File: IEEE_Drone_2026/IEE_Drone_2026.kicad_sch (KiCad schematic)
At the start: 40 parts, among them IC1 TPSM84209RKHT, J1 ESC, J10 M2, J11 Conn_01x02_Socket, J12 RF, J13 USB_C_Receptacle_USB2.0_16P, J2 M4 Mounting, J3 M4 Mounting, J4 M4 Mounting, J5 M4 Mounting, J6 Pixy2, J7 M2, J8 M2, J9 M2, Q1 2N2222, U2 STM32F405RGTx, U3 BMP390, U4 SAM-M10Q-00B, U5 LIS2MDL, Y1 LFXTAL020423, Y2 ABMM2-32.768MHZ-E2F-T

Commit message: wired the imu
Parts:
- added C1: 0.1uF, Capacitor_SMD:C_0603_1608Metric_Pad1.08x0.95mm_HandSolder, symbol Device:C
- added C13: 2.2uF, Capacitor_SMD:C_0603_1608Metric_Pad1.08x0.95mm_HandSolder, symbol Device:C
- added C14: 10nF, Capacitor_SMD:C_0603_1608Metric_Pad1.08x0.95mm_HandSolder, symbol Device:C
- added R6, R8: 5.1k, Resistor_SMD:R_0603_1608Metric_Pad0.98x0.95mm_HandSolder, symbol Device:R
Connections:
- net +3.3V: now also MT1.5 (VDDIO), MT1.8 (VDD), C1.1, C13.1, C14.2
- net GND: now also J13.A1 (GND), J13.A12 (GND), J13.B1 (GND), J13.B12 (GND), J13.S1 (SHIELD), MT1.2 (RESV), MT1.6 (GND), MT1.7 (RESV__2), C1.2, C13.2, C14.1, R6.1, R8.1
- net SCK: no longer U3.2 (SCK)
- net +5V: now reaches J13.A4 (VBUS), J13.A9 (VBUS), J13.B4 (VBUS), J13.B9 (VBUS)
- net at J13.A5 (CC1): now also R6.2
- net PA12: now reaches J13.A6 (D+)
- net PA12: now also J13.B6 (D+), U2.45 (PA12)
- net PA11: now reaches J13.A7 (D-)
- net PA11: now also J13.B7 (D-), U2.44 (PA11)
- net at J13.B5 (CC2): now also R8.2
- net MOSI (SPI3): now reaches MT1.1 (AP_SDO/AP_AD0)
- net MOSI (SPI3): now also U2.53 (PC12)
- net PB7: now reaches MT1.12 (AP_CS)
- net PB7: now also U2.59 (PB7)
- net SCK (SPI3): now reaches MT1.13 (AP_SCL/AP_SCLK)
- net SCK (SPI3): now also U2.51 (PC10)
- net MISO (SPI3): now reaches MT1.14 (AP_SDA/AP_SDIO/AP_SDI)
- net MISO (SPI3): now also U2.52 (PC11)
- net PB8: now reaches MT1.4 (INT1/INT)
- net PB8: now also U2.61 (PB8)
- net PB9: now reaches MT1.9 (INT2/FSYNC)
- net PB9: now also U2.62 (PB9)
- net SCK(SPI1): now reaches U2.21 (PA5)
- net SCK(SPI1): now also U3.2 (SCK)
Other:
- note added: "differentials!!"
- moved on the sheet: MT1, U4

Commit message: start pcb
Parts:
- removed U4: SAM-M10Q-00B, SAM-M10Q-00B:XCVR_SAM-M10Q-00B, symbol 10mq:SAM-M10Q-00B
- added C15, C16, C17, C18, C22: 100nF, Capacitor_SMD:C_0603_1608Metric_Pad1.08x0.95mm_HandSolder, symbol Device:C
- added C19: 4.7uF, Capacitor_SMD:C_0603_1608Metric_Pad1.08x0.95mm_HandSolder, symbol Device:C
- added C20, C21: 2.2uF, Capacitor_SMD:C_0603_1608Metric_Pad1.08x0.95mm_HandSolder, symbol Device:C
- added TP1, TP2: TestPoint, TestPoint:TestPoint_Loop_D2.50mm_Drill1.0mm, symbol Connector:TestPoint
- MT1: footprint ICM-42605:XDCR_ICM-42605 -> forICM:XDCR_ICM-42605
- U3: footprint 10LGA_2X2X0p75_BOS -> bmp390:10LGA_2X2X0p75_BOS
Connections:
- net GND: now also U2.12 (VSSA), U2.18 (VSS), U2.63 (VSS), C15.2, C16.2, C17.2, C18.2, C19.2, C20.2, C21.2, C22.2
- net at U2.1 (VBAT): now also U2.13 (VDDA), U2.19 (VDD), U2.32 (VDD), U2.48 (VDD), U2.64 (VDD), C15.1, C16.1, C17.1, C18.1, C19.1, C22.1
- net at U2.31 (VCAP_1): now also C21.1
- net at U2.47 (VCAP_2): now also C20.1
- net at U2.60 (BOOT0): now also TP1.1
- net at U2.7 (NRST): now also TP2.1
- no-connect marks 3 -> 29
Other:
- note added: "ADD TP's"

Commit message: made power module and removed switch
we don't need a switch. we can just say we will unplug the battery, and if we need a "SWITCH" we will just solder a physical one or sm
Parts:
- removed S1: SKTHAHE010, SKTHAHE010, symbol 16vbig:SKTHAHE010

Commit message: updated connector and moved voltage reg
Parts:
- J1: footprint Connector_PinHeader_1.00mm:PinHeader_1x06_P1.00mm_Vertical -> Connector_JST:JST_SHL_SM08B-SHLS-TF_1x08-1MP_P1.00mm_Horizontal
- Y1: footprint LFXTAL020423:WE-XTAL_HC49_4HSMX -> forICM:WE-XTAL_HC49_4HSMX
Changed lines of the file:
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@@
 			)
 		)
-		(property "Footprint" "Connector_PinHeader_1.00mm:PinHeader_1x06_P1.00mm_Vertical"
+		(property "Footprint" "Connector_JST:JST_SHL_SM08B-SHLS-TF_1x08-1MP_P1.00mm_Horizontal"
 			(at 180.34 20.32 0)
 			(effects
@@
 			)
 		)
-		(property "Footprint" "LFXTAL020423:WE-XTAL_HC49_4HSMX"
+		(property "Footprint" "forICM:WE-XTAL_HC49_4HSMX"
 			(at 29.21 83.82 0)
 			(effects

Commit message: further design
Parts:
- removed C5, C6: 22pF, Capacitor_SMD:C_0603_1608Metric_Pad1.08x0.95mm_HandSolder, symbol Device:C
- removed Y1: LFXTAL020423, forICM:WE-XTAL_HC49_4HSMX, symbol 8mhz crystal:LFXTAL020423
- C2: value 6.8uF -> 10uF
- J13: footprint (none) -> Connector_USB:USB_C_Receptacle_GCT_USB4105-xx-A_16P_TopMnt_Horizontal
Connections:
- net +5V is gone; now on net +VDC: J13.A4 (VBUS), J13.A9 (VBUS), J13.B4 (VBUS), J13.B9 (VBUS)
- net PA11 renamed D-
- net PA12 renamed D+
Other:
- note added: "okay this is 5V in, we need to adjust the power supply to work w/ 5V in but this will go to VDC now instead of just 5V"

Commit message: general wiring & fixes
fixed VDD and VDDIO being grounded... not tied to 3v3dc
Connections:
- net +3.3V: now also C11.2, U5.10 (Vdd_IO), U5.9 (Vdd)
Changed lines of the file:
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@@
+	(wire
+		(pts
+			(xy 259.08 114.3) (xy 259.08 121.92)
+		)
+		(stroke
+			(width 0)
+			(type default)
+		)
+	)
 	(wire
 		(pts
@@
 		(effects
 			(font
+				(size 1.27 1.27)
+			)
+			(justify left bottom)
+		)
+	)
+	(label "+3.3V"
+		(at 259.08 114.3 0)
+		(effects
+			(font

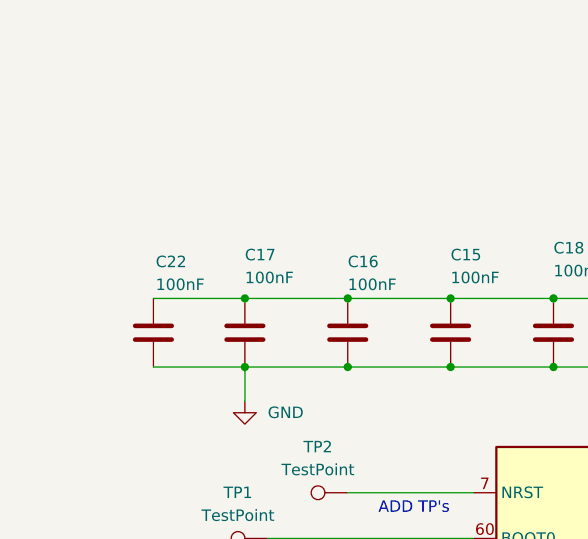
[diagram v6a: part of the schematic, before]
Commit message: added pwr on MCU cap bus
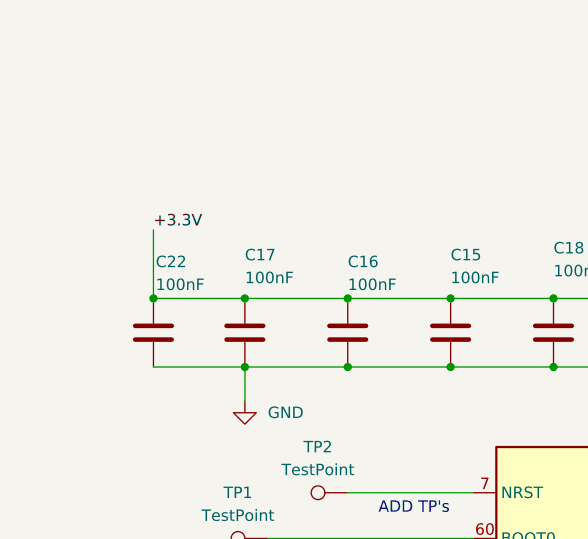
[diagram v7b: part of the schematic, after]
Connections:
- net +3.3V: now also C15.1, C16.1, C17.1, C18.1, C19.1, C22.1, U2.1 (VBAT), U2.13 (VDDA), U2.19 (VDD), U2.32 (VDD), U2.48 (VDD), U2.64 (VDD)
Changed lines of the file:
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@@
+	)
+	(junction
+		(at 17.78 45.72)
+		(diameter 0)
+		(color 0 0 0 0)
 	)
 	(junction
@@
 		(pts
 			(xy 43.18 128.27) (xy 53.34 128.27)
+		)
+		(stroke
+			(width 0)
+			(type default)
+		)
+	)
+	(wire
+		(pts
+			(xy 17.78 38.1) (xy 17.78 45.72)
 		)
 		(stroke
@@
 		(effects
 			(font
+				(size 1.27 1.27)
+			)
+			(justify left bottom)
+		)
+	)
+	(label "+3.3V"
+		(at 17.78 38.1 0)
+		(effects
+			(font

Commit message: some routing updates
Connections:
- net +3.3V: no longer U2.1 (VBAT)
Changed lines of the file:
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@@
 	)
 	(junction
+		(at 46.99 53.34)
+		(diameter 0)
+		(color 0 0 0 0)
+	)
+	(junction
 		(at 375.92 180.34)
 		(diameter 0)
@@
 	)
 	(junction
-		(at 370.84 116.84)
-		(diameter 0)
-		(color 0 0 0 0)
-	)
-	(junction
 		(at 223.52 138.43)
 		(diameter 0)
@@
 	)
 	(junction
-		(at 17.78 45.72)
-		(diameter 0)
-		(color 0 0 0 0)
-	)
-	(junction
 		(at 62.23 45.72)
 		(diameter 0)
@@
 	)
 	(junction
+		(at 81.28 57.15)
+		(diameter 0)
+		(color 0 0 0 0)
+	)
+	(junction
 		(at 39.37 53.34)
 		(diameter 0)
@@
 	)
 	(junction
-		(at 81.28 57.15)
-		(diameter 0)
-		(color 0 0 0 0)
-	)
-	(junction
-		(at 71.12 57.15)
+		(at 342.9 26.67)
 		(diameter 0)
 		(color 0 0 0 0)
 	)
 	(junction
-		(at 342.9 26.67)
+		(at 46.99 45.72)
 		(diameter 0)
 		(color 0 0 0 0)
@@
 	(wire
 		(pts
-			(xy 27.94 53.34) (xy 27.94 57.15)
-		)
-		(stroke
-			(width 0)
-			(type default)
-		)
-	)
-	(wire
-		(pts
 			(xy 365.76 134.62) (xy 365.76 144.78)
 		)
@@
 	(wire
 		(pts
-			(xy 372.11 116.84) (xy 370.84 116.84)
-		)
-		(stroke
-			(width 0)
-			(type default)
-		)
-	)
-	(wire
-		(pts
 			(xy 320.04 191.77) (xy 323.85 191.77)
 		)
@@
 	(wire
 		(pts
-			(xy 71.12 57.15) (xy 68.58 57.15)
-		)
-		(stroke
-			(width 0)
-			(type default)
-		)
-	)
-	(wire
-		(pts
 			(xy 372.11 189.23) (xy 375.92 189.23)
 		)
@@
 	(wire
 		(pts
+			(xy 46.99 53.34) (xy 46.99 58.42)
+		)
+		(stroke
+			(width 0)
+			(type default)
+		)
+	)
+	(wire
+		(pts
 			(xy 342.9 26.67) (xy 342.9 29.21)
 		)
@@
 	(wire
 		(pts
-			(xy 39.37 45.72) (xy 50.8 45.72)
+			(xy 39.37 45.72) (xy 46.99 45.72)
 		)
 		(stroke
@@
 	(wire
 		(pts
-			(xy 68.58 57.15) (xy 68.58 59.69)
+			(xy 46.99 120.65) (xy 53.34 120.65)
 		)
 		(stroke
@@
 	(wire
 		(pts
-			(xy 46.99 120.65) (xy 53.34 120.65)
+			(xy 271.78 140.97) (xy 275.59 140.97)
 		)
 		(stroke
@@
 	(wire
 		(pts
-			(xy 271.78 140.97) (xy 275.59 140.97)
+			(xy 93.98 130.81) (xy 97.79 130.81)
 		)
 		(stroke
@@
 	(wire
 		(pts
-			(xy 93.98 130.81) (xy 97.79 130.81)
+			(xy 46.99 38.1) (xy 46.99 45.72)
 		)
 		(stroke
@@
 	(wire
 		(pts
+			(xy 81.28 45.72) (xy 81.28 57.15)
+		)
+		(stroke
+			(width 0)
+			(type default)
+		)
+	)
+	(wire
+		(pts
 			(xy 223.52 135.89) (xy 246.38 135.89)
 		)
@@
 	(wire
 		(pts
-			(xy 93.98 133.35) (xy 97.79 133.35)
+			(xy 46.99 45.72) (xy 50.8 45.72)
 		)
 		(stroke
@@
 	(wire
 		(pts
-			(xy 177.8 27.94) (xy 171.45 27.94)
+			(xy 93.98 133.35) (xy 97.79 133.35)
 		)
 		(stroke
@@
 	(wire
 		(pts
-			(xy 93.98 87.63) (xy 100.33 87.63)
+			(xy 177.8 27.94) (xy 171.45 27.94)
 		)
 		(stroke
@@
 	(wire
 		(pts
-			(xy 81.28 45.72) (xy 81.28 57.15)
+			(xy 93.98 87.63) (xy 100.33 87.63)
 		)
 		(stroke
@@
 	(wire
 		(pts
-			(xy 17.78 38.1) (xy 17.78 45.72)
-		)
-		(stroke
-			(width 0)
-			(type default)
-		)
-	)
-	(wire
-		(pts
 			(xy 358.14 49.53) (xy 358.14 50.8)
 		)
@@
 	(wire
 		(pts
+			(xy 46.99 53.34) (xy 50.8 53.34)
+		)
+		(stroke
+			(width 0)
+			(type default)
+		)
+	)
+	(wire
+		(pts
 			(xy 46.99 113.03) (xy 53.34 113.03)
 		)
@@
 	(wire
 		(pts
-			(xy 39.37 53.34) (xy 50.8 53.34)
+			(xy 39.37 53.34) (xy 46.99 53.34)
 		)
 		(stroke
@@
 	)
 	(label "+3.3V"
-		(at 372.11 116.84 0)
+		(at 370.84 116.84 0)
 		(effects
 			(font
@@
 		)
 	)
-	(label "+3.3V"
-		(at 17.78 38.1 0)
-		(effects
-			(font
-				(size 1.27 1.27)
-			)
-			(justify left bottom)
-		)
-	)
 	(label "SDA (I2C3)"
 		(at 46.99 113.03 180)
@@
 	(symbol
 		(lib_id "power:GND")
-		(at 27.94 57.15 0)
+		(at 46.99 58.42 0)
 		(unit 1)
 		(exclude_from_sim no)
@@
 		(fields_autoplaced yes)
 		(property "Reference" "#PWR030"
-			(at 27.94 63.5 0)
+			(at 46.99 64.77 0)
 			(effects
 				(font
@@
 		)
 		(property "Value" "GND"
-			(at 30.48 58.4199 0)
+			(at 49.53 59.6899 0)
 			(effects
 				(font
@@
 		)
 		(property "Footprint" ""
-			(at 27.94 57.15 0)
+			(at 46.99 58.42 0)
 			(effects
 				(font
@@
 		)
 		(property "Datasheet" ""
-			(at 27.94 57.15 0)
+			(at 46.99 58.42 0)
 			(effects
 				(font
@@
 		)
 		(property "Description" "Power symbol creates a global label with name \"GND\" , ground"
-			(at 27.94 57.15 0)
+			(at 46.99 58.42 0)
 			(effects
 				(font
@@
 					(unit 1)
 				)
+			)
+		)
+	)
+	(symbol
+		(lib_id "power:+3.3V")
+		(at 46.99 38.1 0)
+		(mirror y)
+		(unit 1)
+		(exclude_from_sim no)
+		(in_bom yes)
+		(on_board yes)
+		(dnp no)
+		(property "Reference" "#PWR04"
+			(at 46.99 41.91 0)
+			(effects
+				(font
+					(size 1.27 1.27)
+				)
+				(hide yes)
+			)
+		)
+		(property "Value" "+3.3V"
+			(at 45.212 33.782 0)
+			(effects
+				(font
+					(size 1.27 1.27)
+				)
+			)
+		)
+		(property "Footprint" ""
+			(at 46.99 38.1 0)
+			(effects
+				(font
+					(size 1.27 1.27)
+				)
+				(hide yes)
+			)
+		)
+		(property "Datasheet" ""
+			(at 46.99 38.1 0)
+			(effects
+				(font
+					(size 1.27 1.27)
+				)
+				(hide yes)
+			)
+		)
+		(property "Description" "Power symbol creates a global label with name \"+3.3V\""
+			(at 46.99 38.1 0)
+			(effects
+				(font
+					(size 1.27 1.27)
+				)
+				(hide yes)
+			)
+		)
+		(pin "1"
+		)
+		(instances
+			(project "IEE_Drone_2026"
+				(path "/3847996a-ac9c-4544-b9d3-a55cb82580af"
+					(reference "#PWR04")
+					(unit 1)
+				)
